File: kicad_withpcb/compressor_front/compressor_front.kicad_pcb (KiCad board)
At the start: 2 copper layers, 35 x 110 mm, 33 parts, among them J1 MAIN BOARD, SW1 BYPASS, SW2 INT/EXT, SW3 HPF DEFEAT, SW4 LINK, U10 LM3915, U9 LM3914

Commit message: Fit real film capacitors on the main board and use Altronics pots for RV5/RV6
RV5 (ATTACK) goes 4k7 -> 10k and RV6 (RELEASE) 500k -> 1M, the nearest
Altronics 9 mm values (R1946, R1950), on the split sheets, both boards
and design.py; the Sim.Params follow (R=10000, R=1e+06).

C5, C8, C9, C10, C14, C15 and C35 were drawn as 7 x 2.5 mm on 5 mm, which
no 2.2-10 uF film part fits. They now use stock KiCad footprints for
in-stock element14 parts:
  10 uF  C5 C8 C15  TDK B32562H1106K000   C_Rect_L16.5mm_W11.8mm_P15.00mm_MKT
  4.7 uF C9 C10     TDK B32562H1475K000   C_Rect_L16.5mm_W7.3mm_P15.00mm_MKT
  2.2 uF C14 C35    KEMET MMK5225K63J06L4 C_Rect_L7.2mm_W7.2mm_P5.00mm_FKS2...

To make room, small parts were re-placed by script (the caps near their
old spots, displaced parts re-homed, then same-footprint parts swapped to
cut wire length; transistors, ICs, connectors and trimmers did not move)
and the main board was re-routed with Freerouting, keeping the original
card-finger stubs. DRC 0 errors, 0 unconnected, schematic parity clean;
ERC 0 errors. The BOM names the element14 parts.
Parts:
- RV5: value 4k7 -> 10k
- RV6: value 500k -> 1M
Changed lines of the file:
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@@
 			)
 		)
-		(property "Value" "500k"
+		(property "Value" "1M"
 			(at 6.05 10.15 90)
 			(layer "F.Fab")
@@
 			)
 		)
-		(property "Value" "4k7"
+		(property "Value" "10k"
 			(at 6.05 10.15 90)
 			(layer "F.Fab")

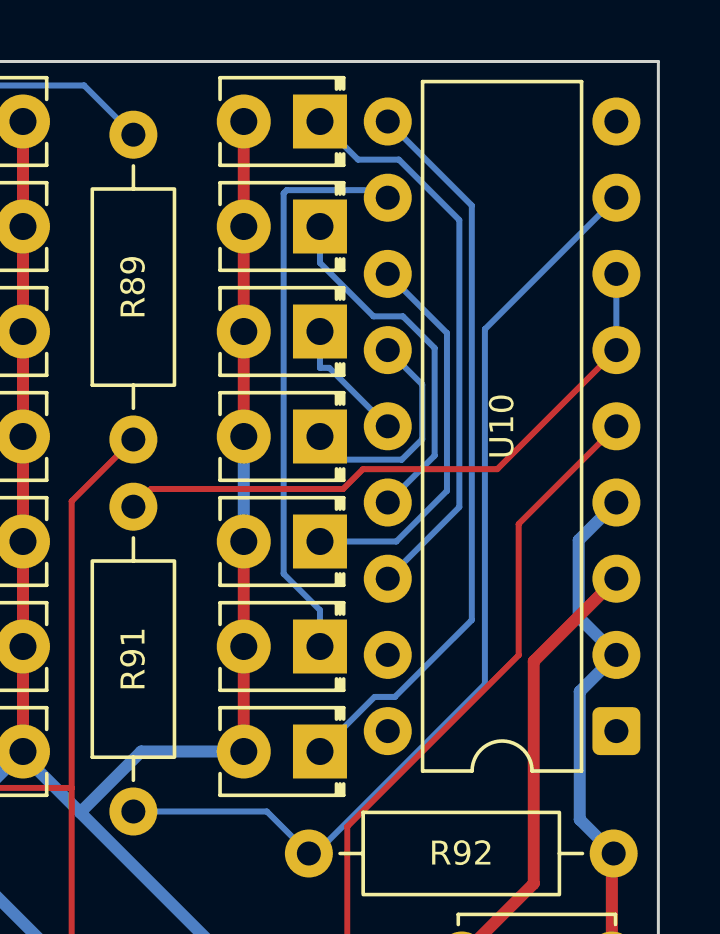
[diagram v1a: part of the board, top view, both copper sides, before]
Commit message: Swap the level meter's LM3915 for an LM3914 on outputs 1-7
Nobody stocks the LM3915, so U10 becomes a second LM3914. The LEDs move
to outputs 1-7 and outputs 8-10 join the top LED, giving a 17 dB scale
with no added parts. Front board LVL tracks re-routed; BOM regenerated.
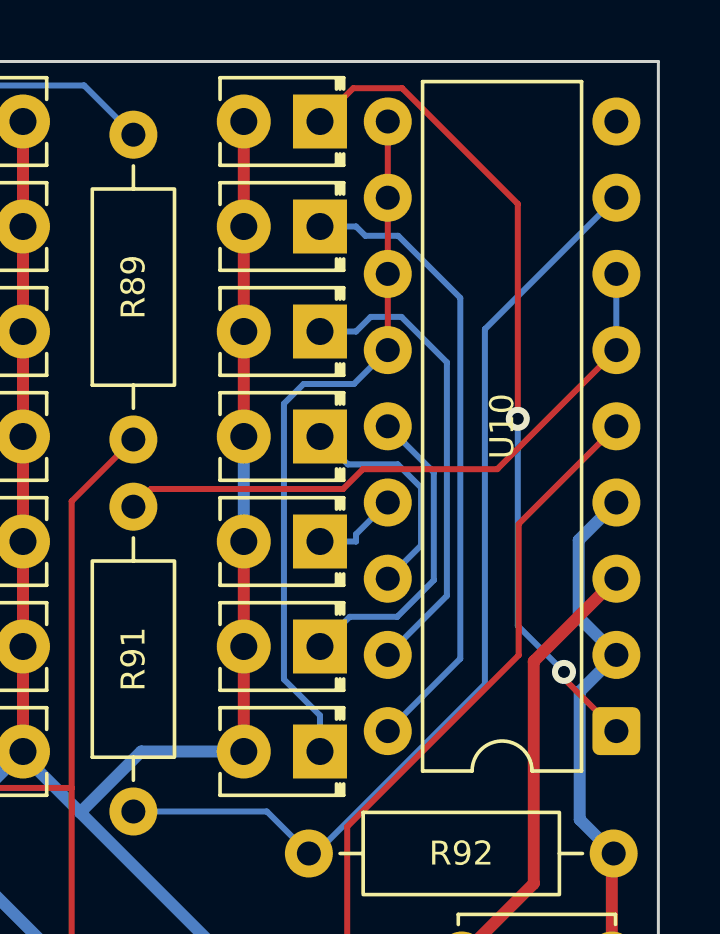
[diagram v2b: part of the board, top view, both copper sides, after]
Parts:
- U10: value LM3915 -> LM3914
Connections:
- U10 pad 1: unconnected-(U10-LED1-Pad1) -> LVL1
- U10 pad 11: LVL6 -> LVL7
- U10 pad 12: LVL5 -> LVL7
- U10 pad 13: LVL4 -> LVL7
- U10 pad 14: LVL3 -> LVL6
- U10 pad 15: LVL2 -> LVL5
- U10 pad 16: LVL1 -> LVL4
- U10 pad 17: unconnected-(U10-LED3-Pad17) -> LVL3
- U10 pad 18: unconnected-(U10-LED2-Pad18) -> LVL2
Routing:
- net LVL3: track 4.28 -> 15.6 mm
- net LVL5: track 13.0 -> 2.94 mm
- net LVL2: track 12.0 -> 21.1 mm
- net LVL6: track 19.2 -> 10.5 mm
- net LVL1: track 18.9 -> 27.6 mm, vias 0 -> 2
- net LVL7: track 24.7 -> 23.9 mm
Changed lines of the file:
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@@
 			)
 		)
-		(property "Value" "LM3915"
+		(property "Value" "LM3914"
 			(at 3.81 22.65 180)
 			(layer "F.Fab")
@@
 			(remove_unused_layers no)
 			(roundrect_rratio 0.15625)
-			(net "unconnected-(U10-LED1-Pad1)")
+			(net "LVL1")
 		)
 		(pad "2" thru_hole circle
@@
 			(layers "*.Cu" "*.Mask")
 			(remove_unused_layers no)
-			(net "LVL6")
+			(net "LVL7")
 		)
 		(pad "12" thru_hole circle
@@
 			(layers "*.Cu" "*.Mask")
 			(remove_unused_layers no)
-			(net "LVL5")
+			(net "LVL7")
 		)
 		(pad "13" thru_hole circle
@@
 			(layers "*.Cu" "*.Mask")
 			(remove_unused_layers no)
-			(net "LVL4")
+			(net "LVL7")
 		)
 		(pad "14" thru_hole circle
@@
 			(layers "*.Cu" "*.Mask")
 			(remove_unused_layers no)
-			(net "LVL3")
+			(net "LVL6")
 		)
 		(pad "15" thru_hole circle
@@
 			(layers "*.Cu" "*.Mask")
 			(remove_unused_layers no)
-			(net "LVL2")
+			(net "LVL5")
 		)
 		(pad "16" thru_hole circle
@@
 			(layers "*.Cu" "*.Mask")
 			(remove_unused_layers no)
-			(net "LVL1")
+			(net "LVL4")
 		)
 		(pad "17" thru_hole circle
@@
 			(layers "*.Cu" "*.Mask")
 			(remove_unused_layers no)
-			(net "unconnected-(U10-LED3-Pad17)")
+			(net "LVL3")
 		)
 		(pad "18" thru_hole circle
@@
 			(layers "*.Cu" "*.Mask")
 			(remove_unused_layers no)
-			(net "unconnected-(U10-LED2-Pad18)")
+			(net "LVL2")
 		)
 		(embedded_fonts no)
@@
 	)
 	(segment
-		(start 129.092 65.1383)
-		(end 129.092 61.5529)
+		(start 126.7817 57.81)
+		(end 126.4717 57.5)
 		(width 0.2)
 		(layer "B.Cu")
@@
 	)
 	(segment
-		(start 127.053 60.4951)
-		(end 125.27 58.7117)
+		(start 127.8768 57.81)
+		(end 126.7817 57.81)
 		(width 0.2)
 		(layer "B.Cu")
@@
 	)
 	(segment
-		(start 125.27 57.5)
-		(end 125.27 58.7117)
+		(start 129.9468 71.9032)
+		(end 129.9468 59.88)
 		(width 0.2)
 		(layer "B.Cu")
@@
 	)
 	(segment
-		(start 129.092 61.5529)
-		(end 128.034 60.4951)
+		(start 127.53 74.32)
+		(end 129.9468 71.9032)
 		(width 0.2)
 		(layer "B.Cu")
@@
 	)
 	(segment
-		(start 128.034 60.4951)
-		(end 127.053 60.4951)
+		(start 125.27 57.5)
+		(end 126.4717 57.5)
 		(width 0.2)
 		(layer "B.Cu")
@@
 	)
 	(segment
-		(start 127.53 66.7)
-		(end 129.092 65.1383)
+		(start 129.9468 59.88)
+		(end 127.8768 57.81)
 		(width 0.2)
 		(layer "B.Cu")
@@
 	)
 	(segment
-		(start 127.53 64.16)
-		(end 125.582 62.2117)
+		(start 127.9851 60.5125)
+		(end 129.5008 62.0282)
+		(width 0.2)
+		(layer "B.Cu")
+		(net "LVL3")
+	)
+	(segment
+		(start 126.4717 61)
+		(end 126.9592 60.5125)
+		(width 0.2)
+		(layer "B.Cu")
+		(net "LVL3")
+	)
+	(segment
+		(start 129.5008 69.8092)
+		(end 127.53 71.78)
+		(width 0.2)
+		(layer "B.Cu")
+		(net "LVL3")
+	)
+	(segment
+		(start 129.5008 62.0282)
+		(end 129.5008 69.8092)
 		(width 0.2)
 		(layer "B.Cu")
@@
 	(segment
 		(start 125.27 61)
-		(end 125.27 62.2117)
+		(end 126.4717 61)
 		(width 0.2)
 		(layer "B.Cu")
@@
 	)
 	(segment
-		(start 125.582 62.2117)
-		(end 125.27 62.2117)
+		(start 126.9592 60.5125)
+		(end 127.9851 60.5125)
 		(width 0.2)
 		(layer "B.Cu")
@@
 	)
 	(segment
-		(start 127.997 65.2723)
-		(end 126.042 65.2723)
+		(start 126.2 65.43)
+		(end 127.8647 65.43)
 		(width 0.2)
 		(layer "B.Cu")
@@
 	)
 	(segment
-		(start 126.042 65.2723)
-		(end 125.27 64.5)
+		(start 128.6397 68.1303)
+		(end 127.53 69.24)
 		(width 0.2)
 		(layer "B.Cu")
@@
 	)
 	(segment
-		(start 127.53 61.62)
-		(end 128.68 62.77)
+		(start 128.6397 66.205)
+		(end 128.6397 68.1303)
 		(width 0.2)
 		(layer "B.Cu")
@@
 	)
 	(segment
-		(start 128.68 62.77)
-		(end 128.68 64.5892)
+		(start 125.27 64.5)
+		(end 126.2 65.43)
 		(width 0.2)
 		(layer "B.Cu")
@@
 	)
 	(segment
-		(start 128.68 64.5892)
-		(end 127.997 65.2723)
+		(start 127.8647 65.43)
+		(end 128.6397 66.205)
 		(width 0.2)
 		(layer "B.Cu")
@@
 	)
 	(segment
-		(start 124.162 56.2883)
-		(end 124.058 56.3918)
+		(start 127.53 64.16)
+		(end 129.0651 65.6951)
 		(width 0.2)
 		(layer "B.Cu")
@@
 	)
 	(segment
-		(start 127.278 56.2883)
-		(end 124.162 56.2883)
+		(start 129.0651 69.2904)
+		(end 127.8455 70.51)
 		(width 0.2)
 		(layer "B.Cu")
@@
 	)
 	(segment
-		(start 125.27 71.5)
-		(end 125.27 70.2883)
+		(start 129.0651 65.6951)
+		(end 129.0651 69.2904)
 		(width 0.2)
 		(layer "B.Cu")
@@
 	)
 	(segment
-		(start 127.53 56.54)
-		(end 127.278 56.2883)
+		(start 127.8455 70.51)
+		(end 126.26 70.51)
 		(width 0.2)
 		(layer "B.Cu")
@@
 	)
 	(segment
-		(start 124.058 56.3918)
-		(end 124.058 69.0766)
+		(start 126.26 70.51)
+		(end 125.27 71.5)
 		(width 0.2)
 		(layer "B.Cu")
@@
 	)
 	(segment
-		(start 124.058 69.0766)
-		(end 125.27 70.2883)
+		(start 128.0083 52.8898)
+		(end 131.8637 56.7452)
+		(width 0.2)
+		(layer "F.Cu")
+		(net "LVL1")
+	)
+	(segment
+		(start 126.3802 52.8898)
+		(end 128.0083 52.8898)
+		(width 0.2)
+		(layer "F.Cu")
+		(net "LVL1")
+	)
+	(segment
+		(start 133.4034 72.5734)
+		(end 133.4034 72.3478)
+		(width 0.2)
+		(layer "F.Cu")
+		(net "LVL1")
+	)
+	(segment
+		(start 131.8637 56.7452)
+		(end 131.8637 63.9106)
+		(width 0.2)
+		(layer "F.Cu")
+		(net "LVL1")
+	)
+	(segment
+		(start 135.15 74.32)
+		(end 133.4034 72.5734)
+		(width 0.2)
+		(layer "F.Cu")
+		(net "LVL1")
+	)
+	(segment
+		(start 125.27 54)
+		(end 126.3802 52.8898)
+		(width 0.2)
+		(layer "F.Cu")
+		(net "LVL1")
+	)
+	(via
+		(at 133.4034 72.3478)
+		(size 0.8)
+		(drill 0.4)
+		(layers "F.Cu" "B.Cu")
+		(net "LVL1")
+	)
+	(via
+		(at 131.8637 63.9106)
+		(size 0.8)
+		(drill 0.4)
+		(layers "F.Cu" "B.Cu")
+		(net "LVL1")
+	)
+	(segment
+		(start 133.4034 72.3478)
+		(end 131.8637 70.8081)
 		(width 0.2)
 		(layer "B.Cu")
-		(net "LVL6")
+		(net "LVL1")
+	)
+	(segment
+		(start 131.8637 70.8081)
+		(end 131.8637 63.9106)
+		(width 0.2)
+		(layer "B.Cu")
+		(net "LVL1")
 	)
 	(segment
@@
 	)
 	(segment
-		(start 130.331 70.618)
-		(end 127.767 73.1813)
+		(start 127.53 61.62)
+		(end 127.53 59.08)
 		(width 0.2)
-		(layer "B.Cu")
+		(layer "F.Cu")
 		(net "LVL7")
 	)
 	(segment
-		(start 130.331 56.8007)
-		(end 130.331 70.618)
+		(start 127.53 59.08)
+		(end 127.53 56.54)
 		(width 0.2)
-		(layer "B.Cu")
+		(layer "F.Cu")
 		(net "LVL7")
 	)
 	(segment
-		(start 127.089 73.1813)
-		(end 125.27 75)
+		(start 127.53 56.54)
+		(end 127.53 54)
 		(width 0.2)
-		(layer "B.Cu")
+		(layer "F.Cu")
 		(net "LVL7")
 	)
 	(segment
-		(start 127.53 54)
-		(end 130.331 56.8007)
+		(start 124.0683 63.4058)
+		(end 124.0683 72.5966)
 		(width 0.2)
 		(layer "B.Cu")
@@
 	)
 	(segment
-		(start 127.767 73.1813)
-		(end 127.089 73.1813)
+		(start 124.0683 72.5966)
+		(end 125.27 73.7983)
 		(width 0.2)
 		(layer "B.Cu")
@@
 	)
 	(segment
-		(start 129.503 66.312)
-		(end 127.815 68)
-		(width 0.2)
-		(layer "B.Cu")
-		(net "LVL5")
-	)
-	(segment
-		(start 127.815 68)
-		(end 125.27 68)
-		(width 0.2)
-		(layer "B.Cu")
-		(net "LVL5")
-	)
-	(segment
-		(start 127.53 59.08)
-		(end 129.503 61.0534)
+		(start 127.53 61.62)
+		(end 126.4 62.75)
 		(width 0.2)
 		(layer "B.Cu")
-		(net "LVL5")
+		(net "LVL7")
 	)
 	(segment
-		(start 129.503 61.0534)
-		(end 129.503 66.312)
+		(start 124.7241 62.75)
+		(end 124.0683 63.4058)
 		(width 0.2)
 		(layer "B.Cu")
-		(net "LVL5")
+		(net "LVL7")
 	)
 	(segment
-		(start 127.899 55.27)
-		(end 129.915 57.2863)
+		(start 126.4 62.75)
+		(end 124.7241 62.75)
 		(width 0.2)
 		(layer "B.Cu")
-		(net "LVL1")
+		(net "LVL7")
 	)
 	(segment
-		(start 129.915 66.8549)
-		(end 127.53 69.24)
+		(start 125.27 75)
+		(end 125.27 73.7983)
 		(width 0.2)
 		(layer "B.Cu")
-		(net "LVL1")
+		(net "LVL7")
 	)
 	(segment
-		(start 125.27 54)
-		(end 126.54 55.27)
+		(start 127.53 66.7)
+		(end 126.4717 67.7583)
 		(width 0.2)
 		(layer "B.Cu")
-		(net "LVL1")
+		(net "LVL5")
 	)
 	(segment
-		(start 126.54 55.27)
-		(end 127.899 55.27)
+		(start 125.27 68)
+		(end 126.4717 68)
 		(width 0.2)
 		(layer "B.Cu")
-		(net "LVL1")
+		(net "LVL5")
 	)
 	(segment
-		(start 129.915 57.2863)
-		(end 129.915 66.8549)
+		(start 126.4717 67.7583)
+		(end 126.4717 68)
 		(width 0.2)
 		(layer "B.Cu")
-		(net "LVL1")
+		(net "LVL5")
 	)
 	(segment

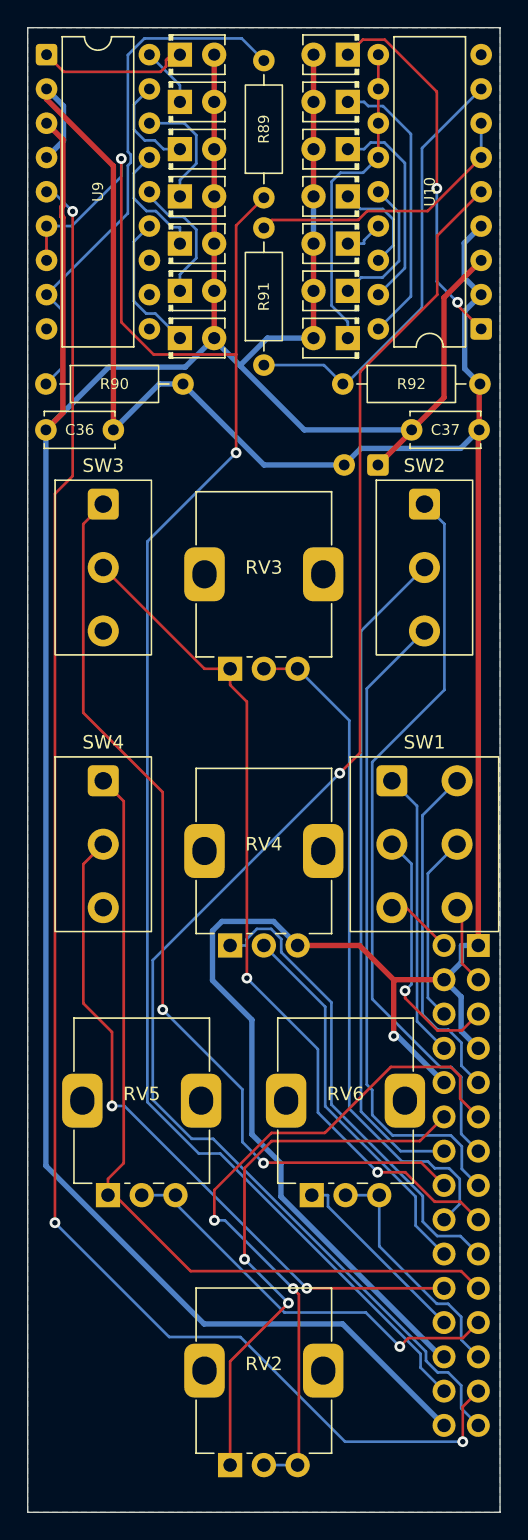
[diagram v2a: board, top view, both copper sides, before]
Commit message: Give both meters ten LEDs and simulate them
Adds D27-D29 (GR outputs 8-10) and D37-D39 (LVL outputs 8-10) on all three
schematics. The front board's meter columns move to a 3.0 mm pitch with
LVL output 10 at the top; R90/R92 move to a 7.62 mm footprint and C38
turns to clear the LEDs; the affected nets were re-routed. R92 becomes 4k7
so RV8 can set the top LED at +18 dBu. The panel gets the six extra holes.
The LM3914 sim model now has its comparators and LED current sinks, and
tools/sim/meters.py simulates both meters.
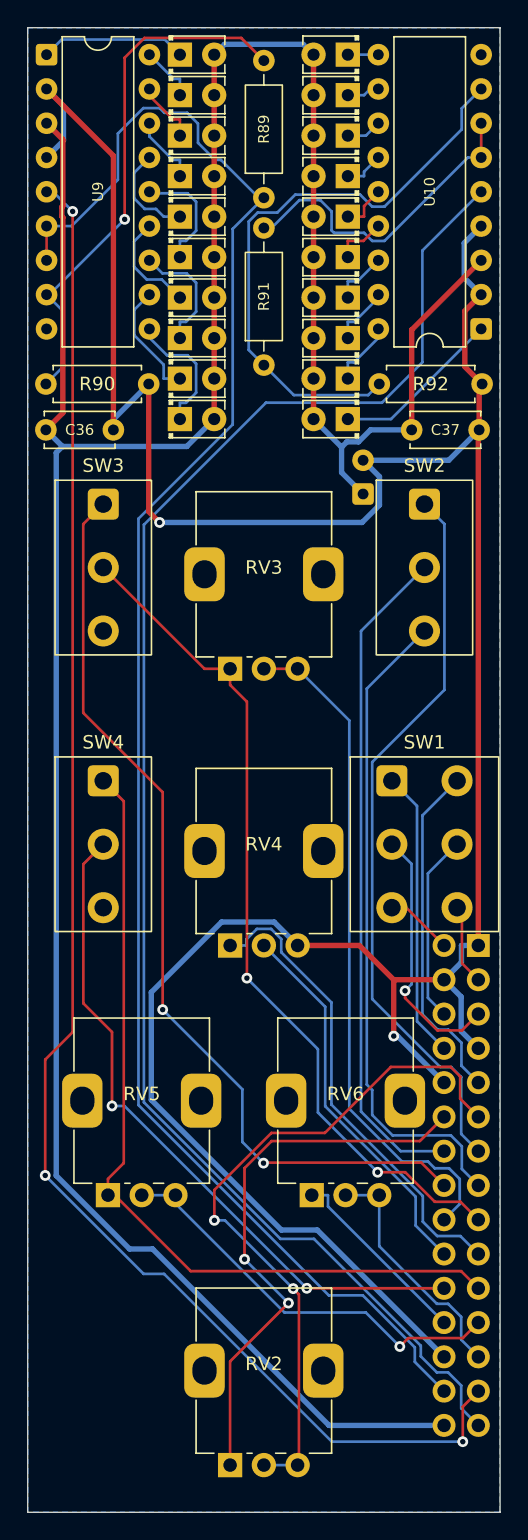
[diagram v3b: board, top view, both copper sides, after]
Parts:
- added D27: meter, LED_THT:LED_D2.0mm_W4.0mm_H2.8mm_FlatTop, F.Cu at (112.8, 75.0)
- added D28: meter, LED_THT:LED_D2.0mm_W4.0mm_H2.8mm_FlatTop, F.Cu at (112.8, 78.0)
- added D29: meter, LED_THT:LED_D2.0mm_W4.0mm_H2.8mm_FlatTop, F.Cu at (112.8, 81.0)
- added D37: meter, LED_THT:LED_D2.0mm_W4.0mm_H2.8mm_FlatTop, F.Cu at (125.3, 60.0)
- added D38: meter, LED_THT:LED_D2.0mm_W4.0mm_H2.8mm_FlatTop, F.Cu at (125.3, 57.0)
- added D39: meter, LED_THT:LED_D2.0mm_W4.0mm_H2.8mm_FlatTop, F.Cu at (125.3, 54.0)
- R90: footprint Resistor_THT:R_Axial_DIN0207_L6.3mm_D2.5mm_P10.16mm_Horizontal -> Resistor_THT:R_Axial_DIN0207_L6.3mm_D2.5mm_P7.62mm_Horizontal
- R92: value 8k2 -> 4k7; footprint Resistor_THT:R_Axial_DIN0207_L6.3mm_D2.5mm_P10.16mm_Horizontal -> Resistor_THT:R_Axial_DIN0207_L6.3mm_D2.5mm_P7.62mm_Horizontal
- moved D30 27.0 mm to (125.3, 81.0)
- moved D31 20.5 mm to (125.3, 78.0)
- moved D32 14.0 mm to (125.3, 75.0)
- moved D36 12.0 mm to (125.3, 63.0)
- moved D33 7.50 mm to (125.3, 72.0)
- moved D35 5.50 mm to (125.3, 66.0)
- moved D26 3.00 mm to (112.8, 72.0)
- moved R92 2.70 mm to (127.6, 78.4)
- moved D25 2.50 mm to (112.8, 69.0)
- moved C38 2.42 mm to (126.4, 86.5), turned to 90 degrees
- moved D24 2.00 mm to (112.8, 66.0)
- moved D23 1.50 mm to (112.8, 63.0)
- moved D22 1.00 mm to (112.8, 60.0)
- moved D34 1.00 mm to (125.3, 69.0)
- moved D21 0.50 mm to (112.8, 57.0)
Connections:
- U10 pad 10: LVL7 -> LVL10
- U10 pad 11: LVL7 -> LVL9
- U10 pad 12: LVL7 -> LVL8
- U9 pad 10: unconnected-(U9-LED10-Pad10) -> GR10
- U9 pad 11: unconnected-(U9-LED9-Pad11) -> GR9
- U9 pad 12: unconnected-(U9-LED8-Pad12) -> GR8
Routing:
- net LVL7: track 23.9 -> 3.02 mm
- net AGND: track 198.7 -> 217.1 mm, vias 1 -> 2
- net LVL2: track 21.1 -> 4.88 mm
- net LVL1: track 27.6 -> 12.6 mm, vias 2 -> 0
- net LVL3: track 15.6 -> 4.44 mm
- net LVL_REFADJ: track 32.7 -> 43.9 mm
- net GR10: track 0.00 -> 9.77 mm
- net GR8: track 0.00 -> 9.01 mm
- net GR9: track 0.00 -> 8.79 mm
- net LVL6: track 10.5 -> 3.48 mm
- net LVL_METER: track 112.9 -> 119.0 mm, vias 1 -> 0
- net GR4: track 8.88 -> 5.16 mm
- net GR_REF: track 134.6 -> 130.9 mm, vias 2 -> 0
- net LVL4: track 7.57 -> 4.11 mm
- net LVL_REF: track 20.8 -> 24.1 mm
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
